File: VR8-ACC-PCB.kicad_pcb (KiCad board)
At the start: 2 copper layers, 140 x 60 mm, 64 parts, among them IC1 LM393P, IC2 VO14642AT, IC3 VO14642AT, IC4 KT12-1A-40L-THT, IC5 NE555P, J1 43650-0516, J2 43650-0516, J3 43650-0216, J4 43650-0416, J5 43045-1013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

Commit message: add some silkscreens
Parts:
- moved QR***** 20.0 mm to (65.5, 88.5)
- moved J4 1.19 mm to (147.5, 90.0)
- moved R18 1.02 mm to (153.5, 71.5)
- moved R21 1.01 mm to (157.0, 71.5)
- moved C1 1.00 mm to (149.5, 71.5)
- moved D11 0.97 mm to (147.0, 83.0)
- moved D10 0.96 mm to (147.0, 78.0)
- moved D7 0.55 mm to (143.5, 55.0)
- moved R17 0.52 mm to (149.5, 54.0)
- moved C2 0.50 mm to (157.5, 54.0)
- moved R19 0.47 mm to (153.5, 54.0)
- moved D8 0.43 mm to (143.5, 62.5)
- moved IC5 0.41 mm to (153.5, 62.5)
- moved D9 0.32 mm to (143.5, 70.0)
- moved PS1 0.29 mm to (133.5, 81.5)
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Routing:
- net SDC_final: track 95.3 -> 123.5 mm
- net GLV_12V: track 92.3 -> 109.5 mm
- net TS-: track 177.2 -> 164.2 mm
- net Net-(D4-A): track 19.5 -> 8.41 mm
- net HV+: track 66.1 -> 55.0 mm, vias 0 -> 2
- net OK_90%: track 28.6 -> 38.9 mm, vias 1 -> 0
- net RTML_enable: track 25.5 -> 17.0 mm
- net Net-(Q2-G): track 25.7 -> 17.5 mm
- net Chassis_Ground: track 29.2 -> 37.0 mm, vias 0 -> 1
- net HV_12V: track 69.5 -> 61.9 mm
- net Net-(Q1-G): track 23.8 -> 30.2 mm
- net IR+_ctrl: track 51.1 -> 45.7 mm, vias 0 -> 1
- net Net-(IC1-1IN+): track 27.6 -> 32.7 mm
- net BATT+: track 99.2 -> 104.0 mm, vias 0 -> 3
- net Net-(IC1-1IN-): track 32.8 -> 36.7 mm, vias 2 -> 1
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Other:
- board text added: "12V"
- board text added: "<60V"
- board text added: "<90%"
- board text added: "BATT+"
- board text added: "CAN-H"
- board text added: "CAN-L"
- board text added: "Chassis"
- board text added: "Finish"
- board text added: "GND"
- board text added: "IMD+"
- board text added: "IMD-"
- board text added: "IMD-H"
- board text added: "IMD-L"
- board text added: "IMD-OK"
- board text added: "IR+"
- board text added: "IR-"
- board text added: "Interlock"
- board text added: "OK"
- board text added: "RTML"
- board text added: "SDC"
- board text added: "SDC-in"
- board text added: "TS+"
- board text added: "TS-"
- board text added: "VI+"
- board text added: "VI-"
- board text added: "VR8-ACC-PCB v1.2.1"
- board text removed: "VR8-ACC-PCB v1.2.0"

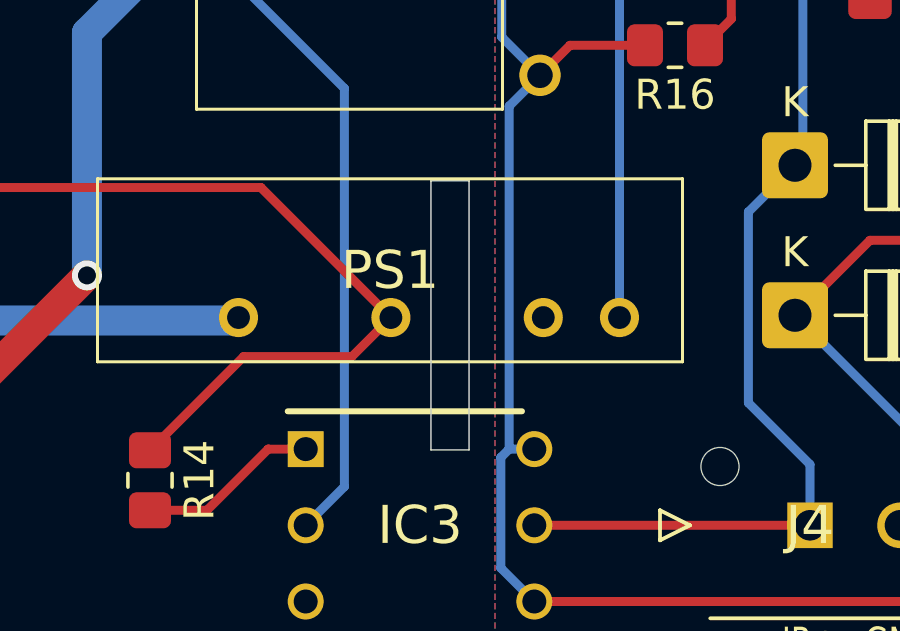
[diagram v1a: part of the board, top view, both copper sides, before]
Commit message: add HV/LV boundary silkscreen
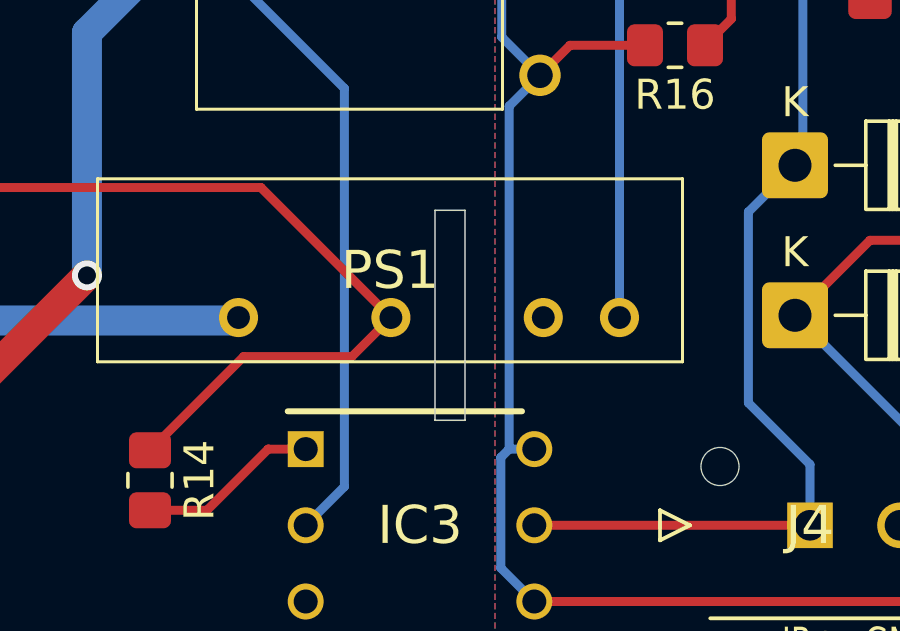
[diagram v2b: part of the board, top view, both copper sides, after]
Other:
- outline, holes or cut-outs redrawn
- board text added: "HV"
- board text added: "LV"
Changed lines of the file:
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@@
+	)
+	(gr_arc
+		(start 135 82)
+		(mid 133.232233 81.267767)
+		(end 132.5 79.5)
+		(stroke
+			(width 0.2)
+			(type solid)
+		)
+		(layer "B.SilkS")
+	)
+	(gr_line
+		(start 132.5 86.5)
+		(end 132.5 95)
+		(stroke
+			(width 0.2)
+			(type solid)
+		)
+		(layer "B.SilkS")
+	)
+	(gr_line
+		(start 135 82)
+		(end 135 84)
+		(stroke
+			(width 0.2)
+			(type solid)
+		)
+		(layer "B.SilkS")
+	)
+	(gr_line
+		(start 132.5 35)
+		(end 132.5 79.5)
+		(stroke
+			(width 0.2)
+			(type solid)
+		)
+		(layer "B.SilkS")
+	)
+	(gr_line
+		(start 137 35)
+		(end 137 95)
+		(stroke
+			(width 0.2)
+			(type solid)
+		)
+		(layer "B.SilkS")
+	)
+	(gr_arc
+		(start 132.5 86.5)
+		(mid 133.232233 84.732233)
+		(end 135 84)
+		(stroke
+			(width 0.2)
+			(type solid)
+		)
+		(layer "B.SilkS")
 	)
 	(gr_arc
@@
 	)
 	(gr_rect
-		(start 134.865 78.515)
-		(end 136.135 87.485)
+		(start 135 79.5)
+		(end 136 86.5)
 		(stroke
 			(width 0.05)
@@
 		)
 		(fill no)
-		(locked yes)
 		(layer "Edge.Cuts")
 	)
@@
 		)
 	)
+	(gr_text "HV"
+		(at 114.5 65 0)
+		(layer "B.SilkS")
+		(effects
+			(font
+				(size 10 10)
+				(thickness 1.25)
+			)
+			(justify mirror)
+		)
+	)
+	(gr_text "LV"
+		(at 155.5 65 0)
+		(layer "B.SilkS")
+		(effects
+			(font
+				(size 10 10)
+				(thickness 1.25)
+			)
+			(justify mirror)
+		)
+	)
+	(dimension
+		(type orthogonal)
+		(layer "B.SilkS")
+		(pts
+			(xy 137 39) (xy 132.5 39.5)
+		)
+		(height 0.5)
+		(orientation 0)
+		(format
+			(prefix "")
+			(suffix "")
+			(units 3)
+			(units_format 1)
+			(precision 4)
+			(suppress_zeroes yes)
+		)
+		(style
+			(thickness 0.2)
+			(arrow_length 1.27)
+			(text_position_mode 2)
+			(arrow_direction outward)
+			(extension_height 0.58642)
+			(extension_offset 0.5)
+			(keep_text_aligned yes)
+		)
+		(gr_text "4.5 mm"
+			(at 125.5 39.5 0)
+			(layer "B.SilkS")
+			(effects
+				(font
+					(size 2 2)
+					(thickness 0.2)
+				)
+				(justify mirror)
+			)
+		)
+	)

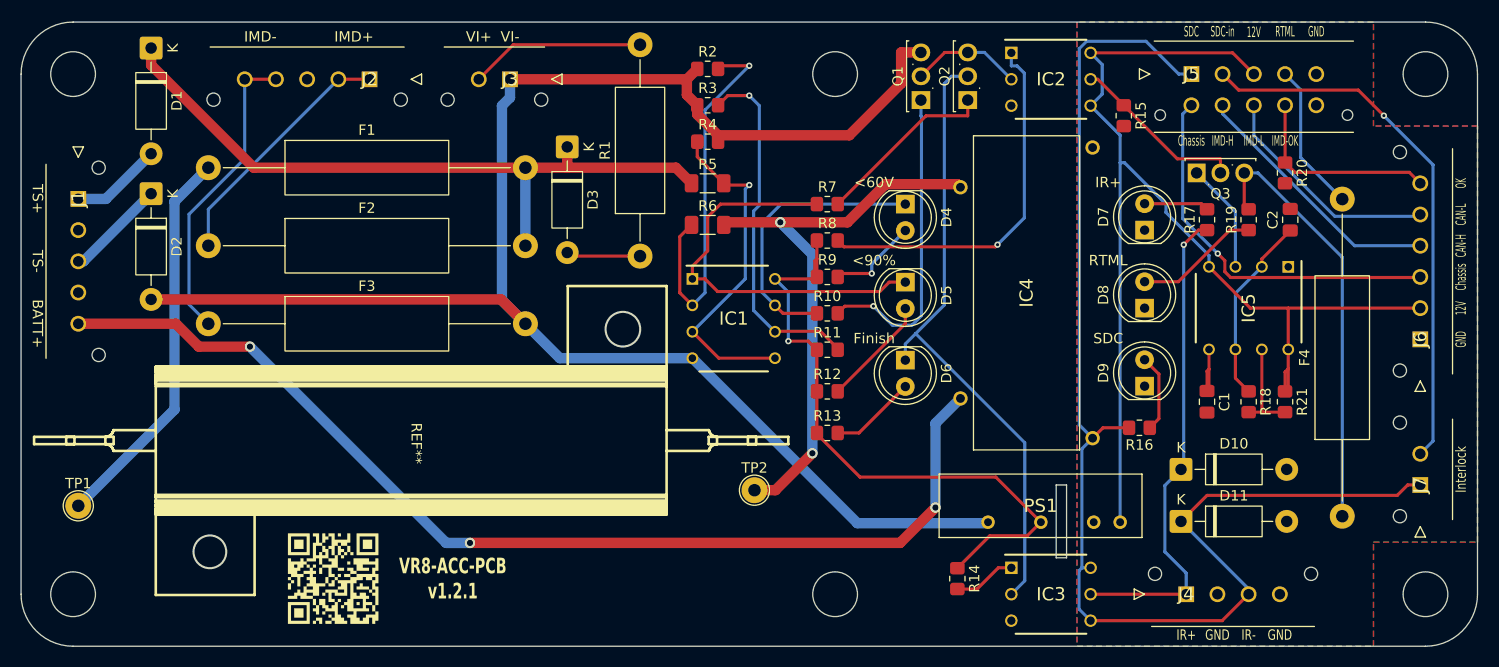
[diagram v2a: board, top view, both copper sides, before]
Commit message: add mouser part numbers
change resisters footprints of 0805 to 1206 for 500V voltage rating
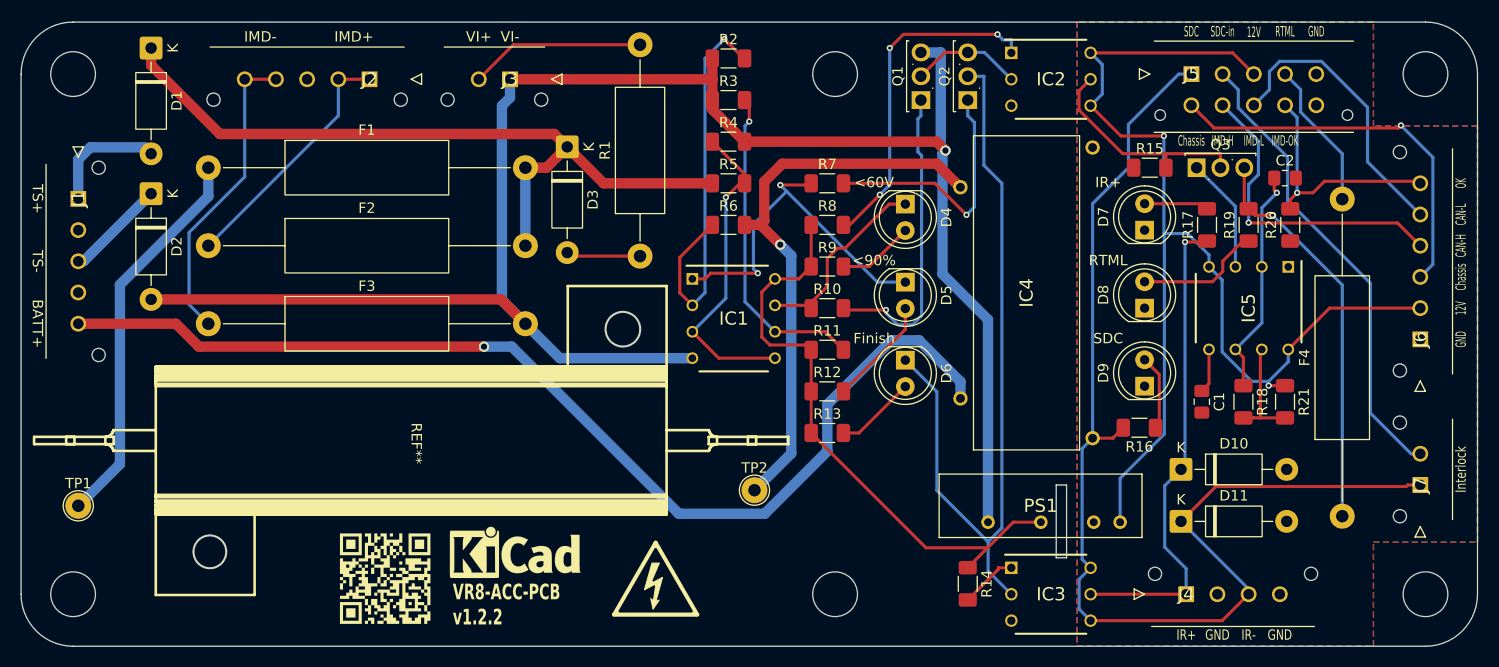
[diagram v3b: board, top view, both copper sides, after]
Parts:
- added REF***: Symbol_HighVoltage_Triangle_8x7mm_Copper, Symbol:Symbol_HighVoltage_Triangle_8x7mm_Copper, F.Cu at (96.5, 88.5)
- added REF**kicad: KiCad-Logo_5mm_SilkScreen, Symbol:KiCad-Logo_5mm_SilkScreen, F.Cu at (83.0, 86.5)
- R10, R12, R13, R14, R15, R16, R17, R18, R19, R20, R21, R7, R8, R9: footprint Resistor_SMD:R_0805_2012Metric_Pad1.20x1.40mm_HandSolder -> Resistor_SMD:R_1206_3216Metric_Pad1.30x1.75mm_HandSolder
- R11: value 47k -> 36k; footprint Resistor_SMD:R_0805_2012Metric_Pad1.20x1.40mm_HandSolder -> Resistor_SMD:R_1206_3216Metric_Pad1.30x1.75mm_HandSolder
- R2: value 100k -> 51k; footprint Resistor_SMD:R_0805_2012Metric_Pad1.20x1.40mm_HandSolder -> Resistor_SMD:R_1206_3216Metric_Pad1.30x1.75mm_HandSolder
- R3: value 6.8k -> 3.3k; footprint Resistor_SMD:R_0805_2012Metric_Pad1.20x1.40mm_HandSolder -> Resistor_SMD:R_1206_3216Metric_Pad1.30x1.75mm_HandSolder
- R4: value 100k -> 56k; footprint Resistor_SMD:R_0805_2012Metric_Pad1.20x1.40mm_HandSolder -> Resistor_SMD:R_1206_3216Metric_Pad1.30x1.75mm_HandSolder
- R6: value 3.9M -> 3.3M
- moved R15 5.59 mm to (144.0, 49.0), turned to 0 degrees
- moved R20 5.02 mm to (157.5, 54.5), turned to 90 degrees
- moved QR***** 5.00 mm to (70.5, 88.5)
- moved C2 4.03 mm to (157.0, 50.0), turned to 0 degrees
- moved R2 2.24 mm to (103.5, 38.5)
- moved R3 2.06 mm to (103.5, 42.5)
- moved R4 2.00 mm to (103.5, 46.5)
- moved R5 2.00 mm to (103.5, 50.5)
- moved R6 2.00 mm to (103.5, 54.5)
- moved R7 2.00 mm to (113.0, 50.5)
- moved R8 1.50 mm to (113.0, 54.5)
- moved R14 1.12 mm to (126.5, 89.0)
- moved R9 1.00 mm to (113.0, 58.5)
- moved C1 0.50 mm to (149.0, 71.5)
- moved Q3 0.50 mm to (148.5, 49.0)
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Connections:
- R15 pad 1: RTML_enable -> GND
- R15 pad 2: GND -> RTML_enable
- R20 pad 1: IMD_Status -> GND
- R20 pad 2: GND -> IMD_Status
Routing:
- net Net-(D6-K): track 60.6 -> 74.3 mm
- net TS-: track 164.2 -> 176.7 mm, vias 0 -> 1
- net SDC_final: track 123.5 -> 112.1 mm
- net OK_60V: track 27.3 -> 18.1 mm
- net SDC_after_MSD: track 52.1 -> 44.9 mm, vias 1 -> 0
- net Net-(Q2-G): track 17.5 -> 24.7 mm, vias 0 -> 1
- net IMD_CAN_L: track 21.9 -> 27.9 mm
- net IMD_CAN_H: track 25.1 -> 30.5 mm, vias 0 -> 1
- net TS+: track 67.8 -> 72.6 mm
- net HV_12V: track 61.9 -> 57.1 mm, vias 1 -> 0
- net RTML_enable: track 17.0 -> 21.5 mm
- net OK_90%: track 38.9 -> 34.6 mm, vias 0 -> 2
- net Net-(IC5-THRES): track 18.2 -> 22.0 mm, vias 0 -> 1
- net IMD_Status: track 19.3 -> 22.8 mm, vias 0 -> 1
- net Net-(IC1-2IN-): track 33.9 -> 30.5 mm
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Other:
- board text added: "VR8-ACC-PCB v1.2.2"
- board text removed: "VR8-ACC-PCB v1.2.1"
